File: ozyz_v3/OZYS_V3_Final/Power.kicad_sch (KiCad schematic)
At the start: 31 parts, among them J1 Conn_01x02_Pin, Q1 AO3401A, Q3 AO3401A, U2 TPS63070RNMR, U3 AMS1117-3.3

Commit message: Yolo2
new Ozys
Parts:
- removed C10, C11, C12, C13, C7, C8, C9: 22u, Capacitor_SMD:C_0603_1608Metric, symbol Device:C
- removed C2, C3, C4, C5: 10u, Capacitor_SMD:C_0603_1608Metric, symbol Device:C
- removed C6: 100n, Capacitor_SMD:C_0402_1005Metric, symbol Device:C
- removed J1: Conn_01x02_Pin, Rocketry_Manual:1054301102, symbol Connector:Conn_01x02_Pin
- removed L2: SPM6530T-1R5M100, Rocketry_Easyeda:IND-SMD_L7.1-W6.5-P5.60, symbol Rocketry_Easyeda:SPM6530T-1R5M100
- removed Q3: AO3401A, Package_TO_SOT_SMD:SOT-23, symbol Transistor_FET:AO3401A
- removed R4: 10k, Resistor_SMD:R_0402_1005Metric, symbol Device:R
- removed R5: 3.9K, Resistor_SMD:R_0603_1608Metric, symbol Device:R
- removed U2: TPS63070RNMR, Rocketry_Easyeda:VQFN-HR-15_L3.0-W2.5-P0.50-BL_TPS63070RNMR, symbol Rocketry_Easyeda:TPS63070RNMR
- removed U3: AMS1117-3.3, Package_TO_SOT_SMD:SOT-223-3_TabPin2, symbol Regulator_Linear:AMS1117-3.3
- added C15, C16, C17: 10u, Capacitor_SMD:C_0603_1608Metric, symbol Device:C
- added C18: 100n, Capacitor_SMD:C_0402_1005Metric, symbol Device:C
- added C19, C20, C21, C23, C25: 22u, Capacitor_SMD:C_0603_1608Metric, symbol Device:C
- added J2: Conn_01x02_Pin, Rocketry_Manual:1054301102, symbol Connector:Conn_01x02_Pin
- added Q2: AO3401A, Package_TO_SOT_SMD:SOT-23, symbol Transistor_FET:AO3401A
- added R13: 150k, Resistor_SMD:R_0603_1608Metric, symbol Device:R
- added R9: 5.1k, Resistor_SMD:R_0402_1005Metric, symbol Device:R
- added U5: TPS63070RNMR, Rocketry_Easyeda:VQFN-HR-15_L3.0-W2.5-P0.50-BL_TPS63070RNMR, symbol Rocketry_Easyeda:TPS63070RNMR
- C14: value 22u -> 10u
- R10: value 130K -> 5.1k; footprint Resistor_SMD:R_0603_1608Metric -> Resistor_SMD:R_0402_1005Metric
- R11: value 680K -> 150K; footprint Resistor_SMD:R_0402_1005Metric -> Resistor_SMD:R_0603_1608Metric
- R12: value 150k -> 470K; footprint Resistor_SMD:R_0603_1608Metric -> Resistor_SMD:R_0402_1005Metric
- R6: value 20K -> 10k
- R7: value 5.1k -> 3.9K; footprint Resistor_SMD:R_0402_1005Metric -> Resistor_SMD:R_0603_1608Metric
- R8: value 5.1k -> 20K
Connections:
- net +3.3V: now also L3.2, R12.2, C17.2, C19.2, C20.2, C21.2
- net +3V3A: now also L3.1, C23.2, C25.2, Q2.2 (S), R13.1; no longer C14.2, R12.1
- net 3V3A_SW: now also Q2.3 (D)
- net 3V3A_SW_EN: now also Q2.1 (G), R13.2; no longer R12.2
- net BAT_V_M: now also R7.2, R8.1; no longer R6.1
- net GND: now also R11.1, C15.1, C16.1, C17.1, C18.2, C19.1, C20.1, C21.1, C23.1, C25.1, J2.2 (Pin_2), R9.1; no longer R8.1
- net at Q1.2 (S): now also C14.2, R6.2, C15.2, C16.2
- net at D1.1 (K), Q1.3 (D): now also R8.2, J2.1 (Pin_1); no longer R6.2
- net at R10.2: now also USB1.10 (CC2); no longer R11.1
- net at R11.2: now also R12.1; no longer L1.1
- net at USB1.4 (CC1): now also R9.2; no longer R7.2
- net +5VA: no longer names the net of L1.2

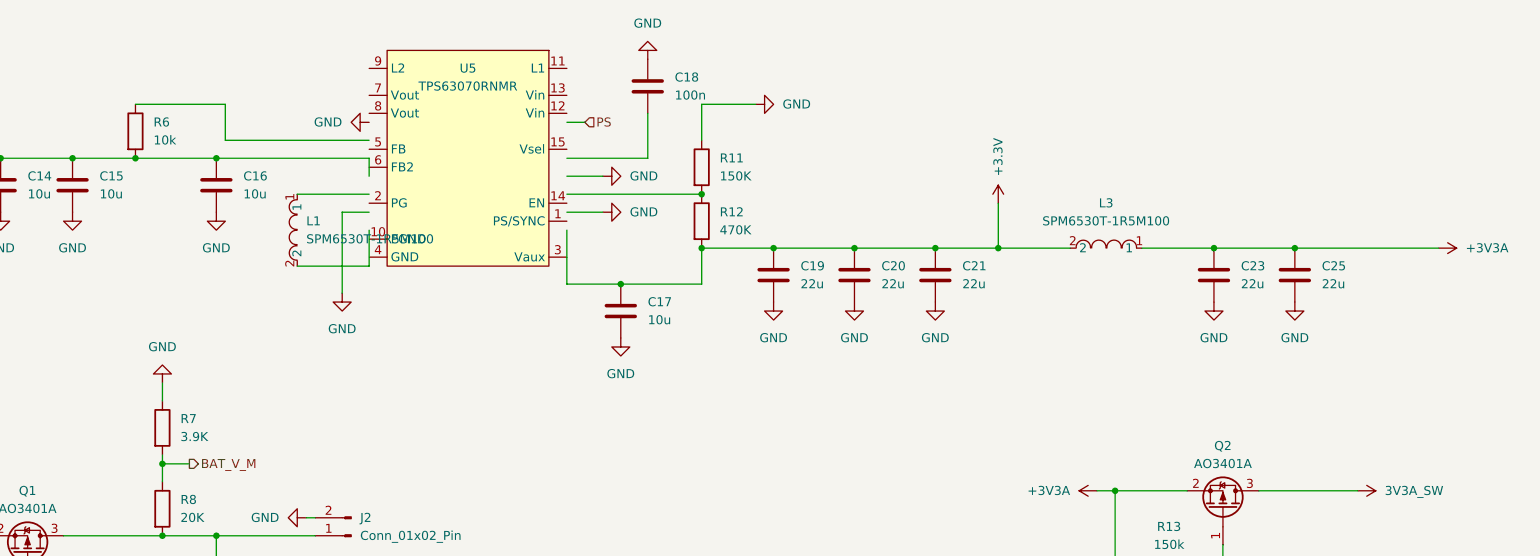
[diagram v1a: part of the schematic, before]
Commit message: OZYS and EPSILON schematics updated.
OZYS
- New 3.5 PJ-320A-4P DIP
- Fixed TPS Regulator Connections
- Fixed STM32 Connections
- Added Associated .ioc for stm32 pin config
- Loading Capacitance of LSE based off  an5093 STM datasheet
EPSILON
- same 3.5 as OZYS
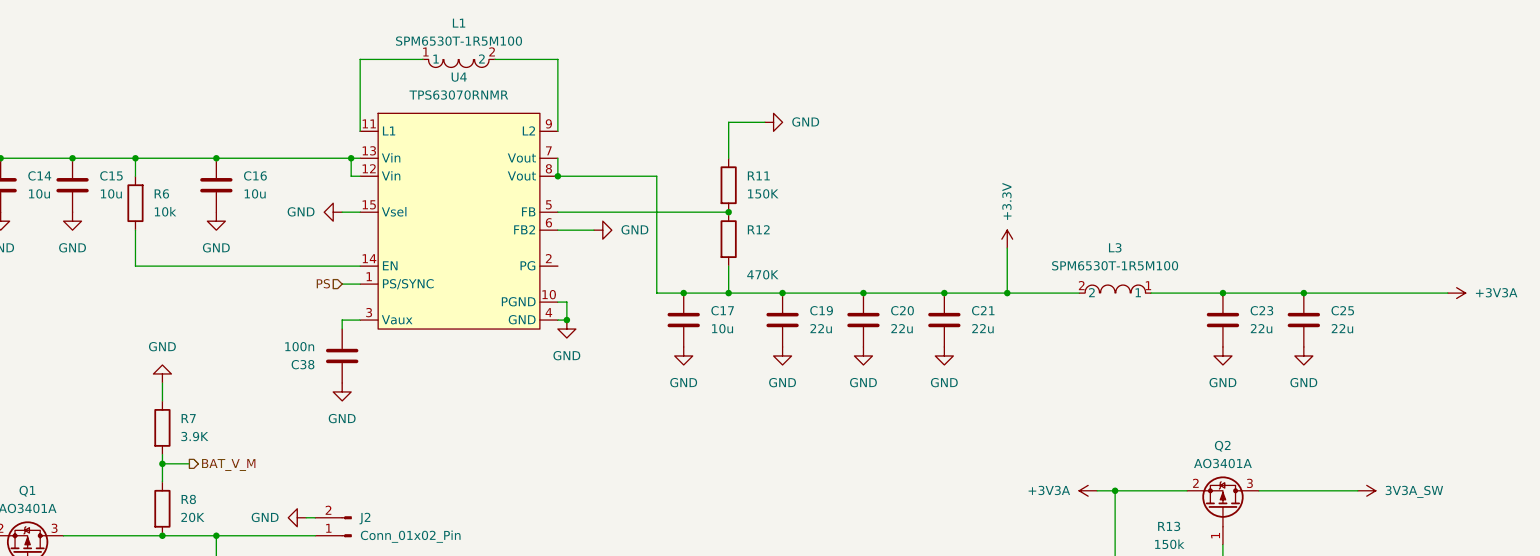
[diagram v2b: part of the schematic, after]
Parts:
- removed C18: 100n, Capacitor_SMD:C_0402_1005Metric, symbol Device:C
- removed U5: TPS63070RNMR, Rocketry_Easyeda:VQFN-HR-15_L3.0-W2.5-P0.50-BL_TPS63070RNMR, symbol Rocketry_Easyeda:TPS63070RNMR
- added C38: 100n, Capacitor_SMD:C_0402_1005Metric, symbol Device:C
- added U4: TPS63070RNMR, Rocketry_Easyeda:VQFN-HR-15_L3.0-W2.5-P0.50-BL_TPS63070RNMR, symbol Rocketry_Easyeda:TPS63070RNMR
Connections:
- net +3.3V: now also U4.7 (Vout), U4.8 (Vout)
- net GND: now also C38.2, U4.10 (PGND), U4.15 (Vsel), U4.4 (GND), U4.6 (FB2)
- net PS: now also U4.1 (PS/SYNC)
- net at C14.2, C15.2, C16.2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: now also U4.12 (Vin), U4.13 (Vin)
- net at R11.2, R12.1: now also U4.5 (FB)
- net at R6.1: now also U4.14 (EN)
- net at L1.1: now also U4.11 (L1)
- net at L1.2: now also U4.9 (L2)
- new net: C38.1, U4.3 (Vaux)
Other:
- moved on the sheet: C17, C19, C20, C21, C23, C25, L3, R11, R12, R6
